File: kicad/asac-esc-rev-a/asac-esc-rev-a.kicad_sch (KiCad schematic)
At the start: 53 parts, among them J1 Conn_01x02_RESET, J14 Conn_01x03, J2 Conn_01x03, J3 Motor, U1 AMS1117-3.3, U2 XJNG2103, U3 STM32C011F6Px, U4 ASDM30DN40E-R, DUAL MOSFET, U5 INA180A3

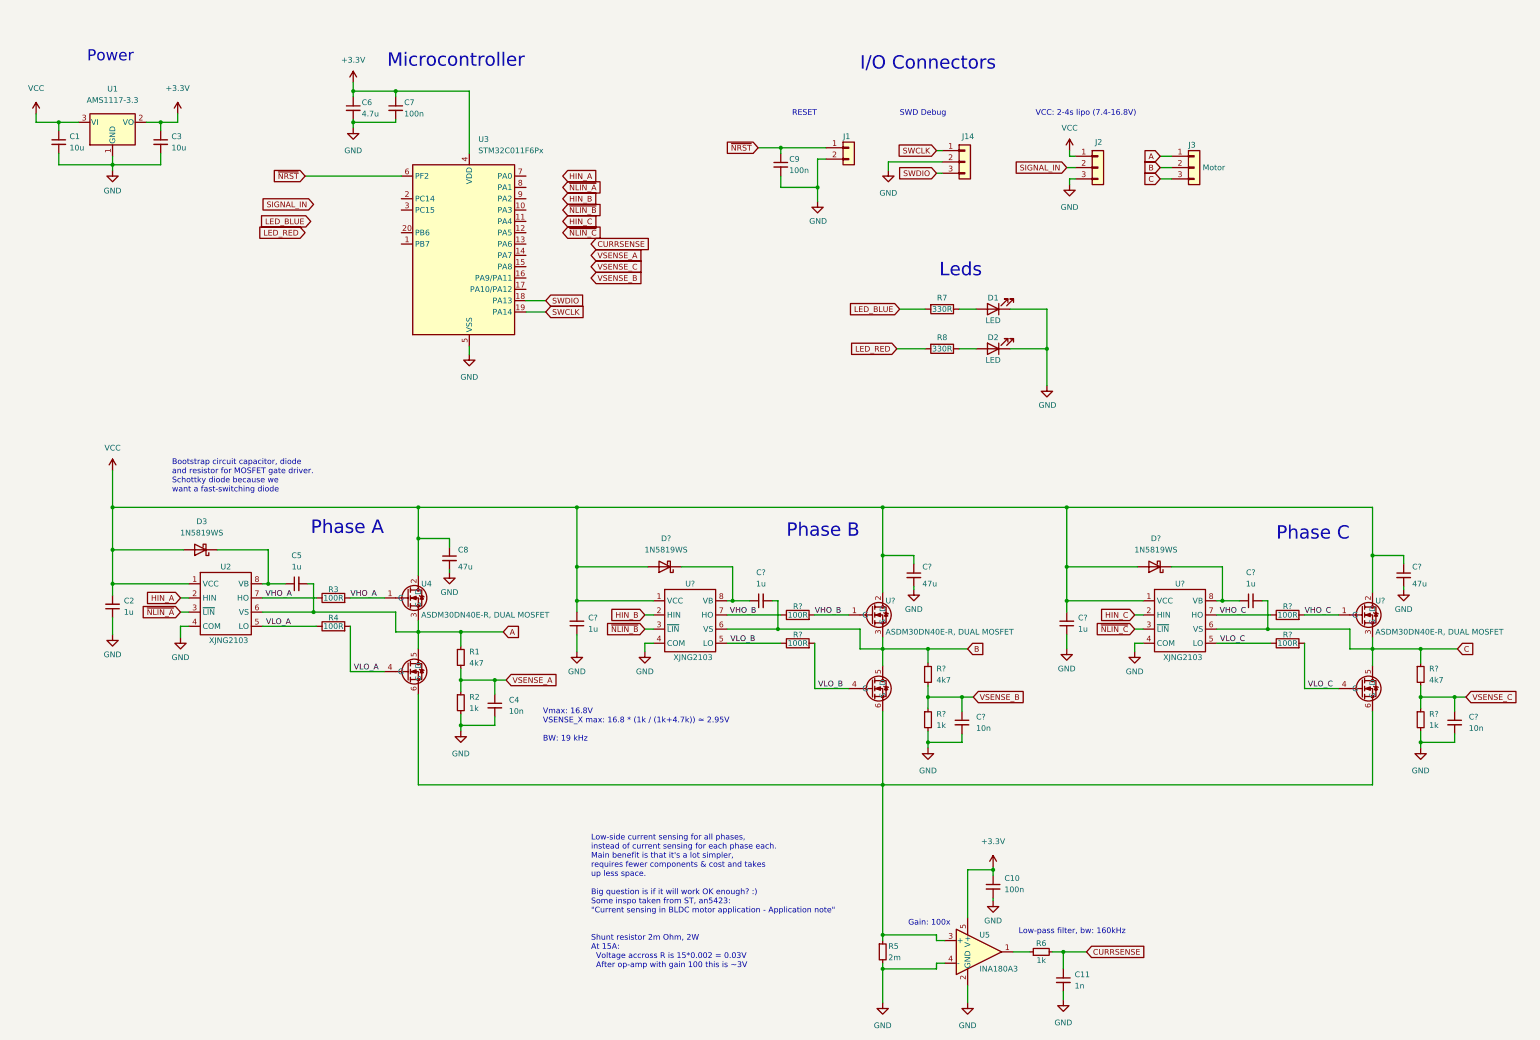
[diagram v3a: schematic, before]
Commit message: Did layout and routing of PCB. Rev. A of the PCB is considered done and I have just done the order for PCB and components :)
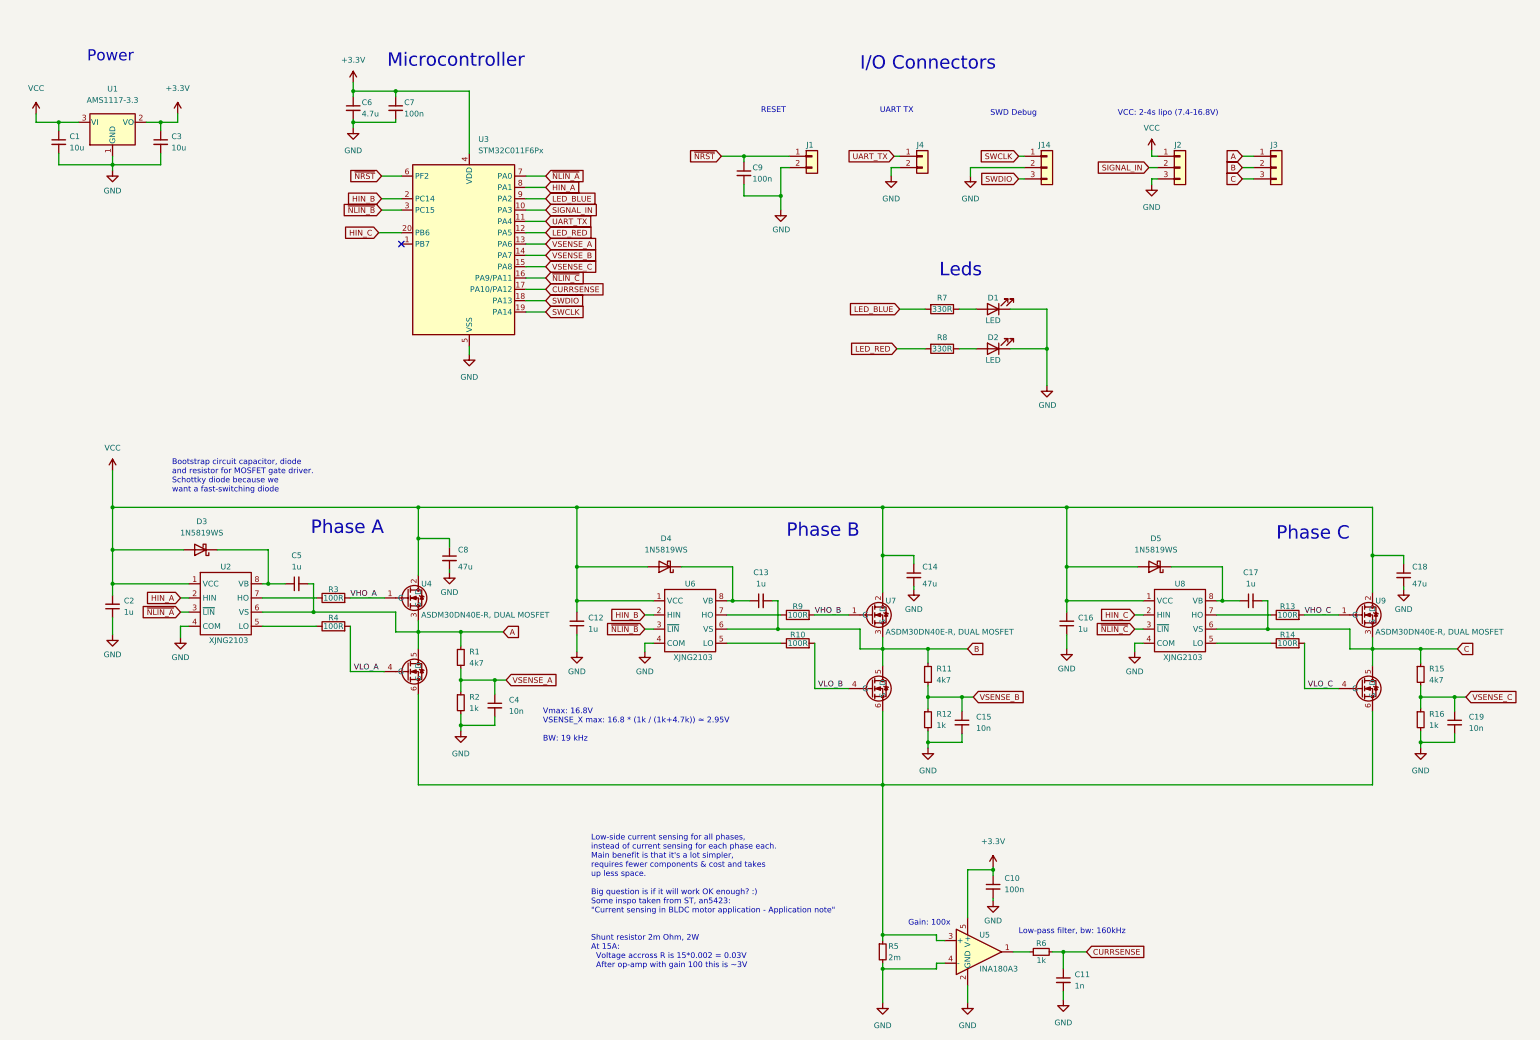
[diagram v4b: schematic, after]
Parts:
- added J4: Conn_01x02_RESET, Custom:PinHeader_1x02_P2.54mm_Vertical_No_silk, symbol Connector_Generic:Conn_01x02
- J1: footprint Custom:PinHeader_1x02_P1.27mm_Vertical_No_Silk -> Custom:PinHeader_1x02_P2.54mm_Vertical_No_silk
- J14: footprint Custom:PinHeader_1x03_P1.27mm_Vertical_no_silk_smd -> Custom:PinSocket_1x03_P2.54mm_Vertical_No_silk
- gave numbers to parts that had none: 22
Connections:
- net CURRSENSE: now also U3.17 (PA10/PA12)
- net GND: now also J4.2 (Pin_2)
- net HIN_A: now also U3.8 (PA1)
- net HIN_B: now also U3.2 (PC14)
- net HIN_C: now also U3.20 (PB6)
- net LED_BLUE: now also U3.9 (PA2)
- net LED_RED: now also U3.12 (PA5)
- net SIGNAL_IN: now also U3.10 (PA3)
- net VHO_A: no longer R3.1, U2.7 (HO)
- net VHO_B: no longer R9.1, U6.7 (HO)
- net VHO_C: no longer R13.1, U8.7 (HO)
- net VLO_A: no longer R4.1, U2.5 (LO)
- net VLO_B: no longer R10.1, U6.5 (LO)
- net VLO_C: no longer R14.1, U8.5 (LO)
- net VSENSE_A: now also U3.13 (PA6)
- net VSENSE_B: now also U3.14 (PA7)
- net VSENSE_C: now also U3.15 (PA8)
- net ~{NLIN_A}: now also U3.7 (PA0)
- net ~{NLIN_B}: now also U3.3 (PC15)
- net ~{NLIN_C}: now also U3.16 (PA9/PA11)
- net UART_TX: now reaches U3.11 (PA4)
- net UART_TX: now also J4.1 (Pin_1)
- new net: R10.1, U6.5 (LO)
- new net: R9.1, U6.7 (HO)
- new net: R4.1, U2.5 (LO)
- new net: R3.1, U2.7 (HO)
- new net: R14.1, U8.5 (LO)
- new net: R13.1, U8.7 (HO)
- no-connect marks 0 -> 1
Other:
- note added: "UART TX"
- moved on the sheet: C9, J1, J14, J2, J3
